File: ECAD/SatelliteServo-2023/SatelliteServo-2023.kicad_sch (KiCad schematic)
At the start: 18 parts, among them J1 Conn_02x05_Odd_Even, J10 Conn_01x03, J11 Conn_01x03, J2 Conn_01x02, J3 Conn_01x03, J4 Conn_01x03, J5 Conn_01x03, J6 Conn_01x03, J7 Conn_01x03, J8 Conn_01x03, J9 Conn_01x03

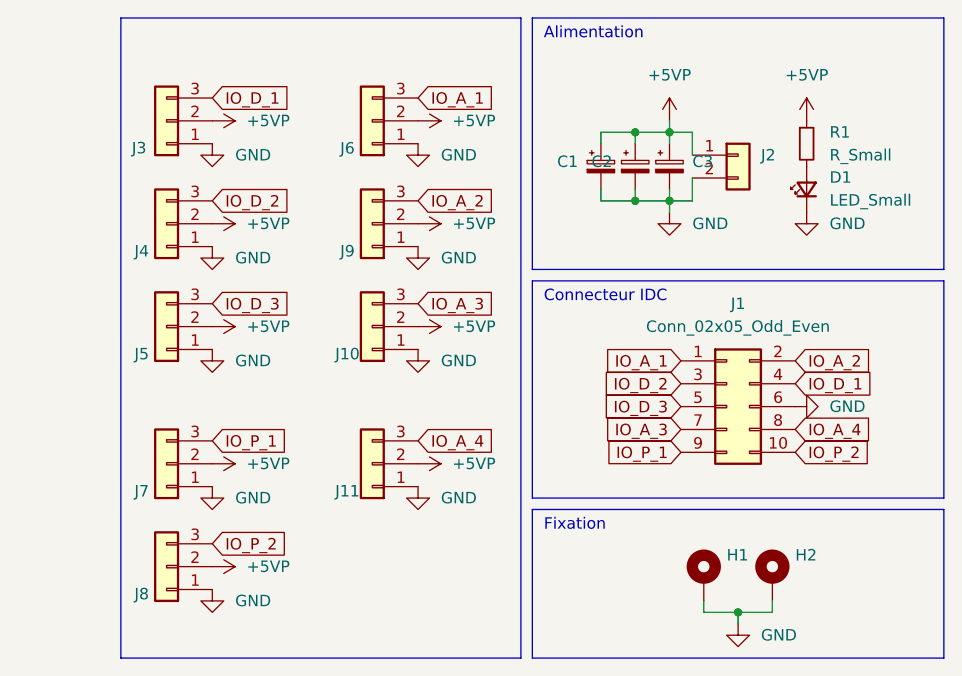
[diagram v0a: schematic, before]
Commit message: Live 146 - Fix servo board
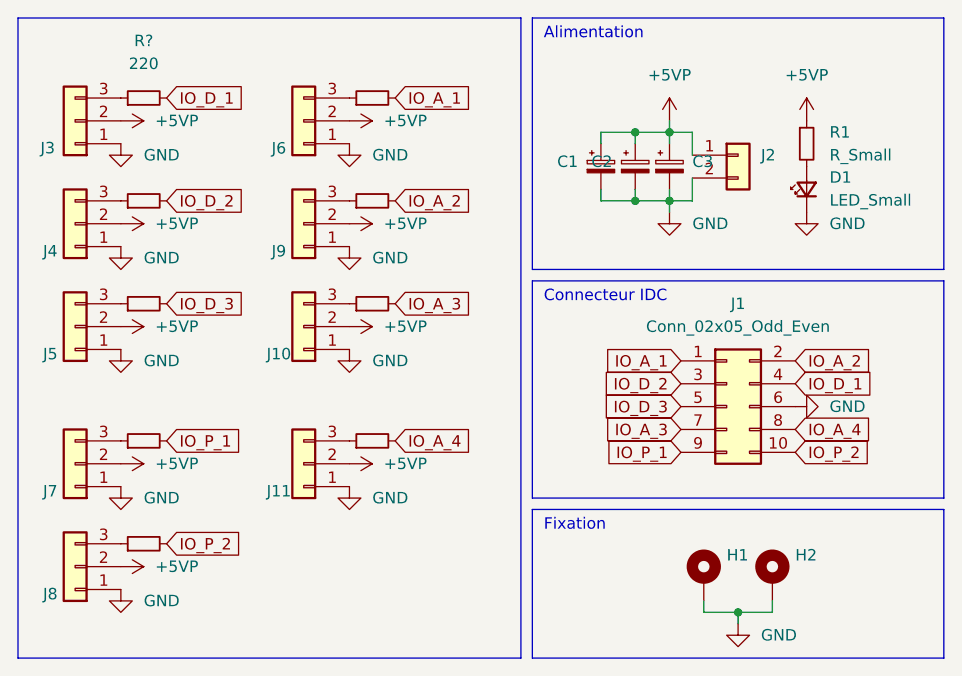
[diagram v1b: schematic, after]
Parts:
- added R? (x9): 220, Resistor_SMD:R_1206_3216Metric_Pad1.30x1.75mm_HandSolder, symbol Device:R_Small
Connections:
- net IO_A_1: now also R?.2; no longer J6.3 (Pin_3)
- net IO_A_2: now also R?.2; no longer J9.3 (Pin_3)
- net IO_A_3: now also R?.2; no longer J10.3 (Pin_3)
- net IO_A_4: now also R?.2; no longer J11.3 (Pin_3)
- net IO_D_1: now also R?.2; no longer J3.3 (Pin_3)
- net IO_D_2: now also R?.2; no longer J4.3 (Pin_3)
- net IO_D_3: now also R?.2; no longer J5.3 (Pin_3)
- net IO_P_1: now also R?.2; no longer J7.3 (Pin_3)
- net IO_P_2: now also R?.2; no longer J8.3 (Pin_3)
- new net: J5.3 (Pin_3), R?.1
- new net: J4.3 (Pin_3), R?.1
- new net: J8.3 (Pin_3), R?.1
- new net: J11.3 (Pin_3), R?.1
- new net: J9.3 (Pin_3), R?.1
- new net: J10.3 (Pin_3), R?.1
- new net: J7.3 (Pin_3), R?.1
- new net: J6.3 (Pin_3), R?.1
- new net: J3.3 (Pin_3), R?.1
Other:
- moved on the sheet: J10, J11, J3, J4, J5, J6, J7, J8, J9
